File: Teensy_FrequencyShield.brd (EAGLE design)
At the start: 17 parts, among them IC9 78L05F

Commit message: Tweaked pin layout; added back in extra DDS & PLL channel names to Teensy pinout
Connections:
- net DDS3_CS: now also TEENSY.26; no longer TEENSY.15/A1
- net DDS3_IOUPDATE: now also TEENSY.28; no longer TEENSY.17/A3
- net DDS3_PS0: now also TEENSY.27; no longer TEENSY.16/A2
- net DDS3_RESET: now also TEENSY.25; no longer TEENSY.14/A0
- net PLL1_LE: now also TEENSY.15/A1; no longer TEENSY.30
- net PLL1_MUX: now also TEENSY.14/A0; no longer TEENSY.26
- net PLL2_LE: now also TEENSY.17/A3; no longer TEENSY.31
- net PLL2_MUX: now also TEENSY.16/A2; no longer TEENSY.27
- net PLL3_LE: now also TEENSY.30; no longer TEENSY.32
- net PLL3_MUX: now also TEENSY.29; no longer TEENSY.28
- net PLL4_LE: now also TEENSY.32; no longer TEENSY.33
- net PLL4_MUX: now also TEENSY.31; no longer TEENSY.29
- net SW1: now also TEENSY.33; no longer TEENSY.25
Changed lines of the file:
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@@
 <?xml version="1.0" encoding="utf-8"?>
 <!DOCTYPE eagle SYSTEM "eagle.dtd">
-<eagle version="6.2">
+<eagle version="6.5.0">
 <drawing>
 <settings>
@@
 </class>
 </classes>
-<designrules>
+<designrules name="default">
 <description language="de">&lt;b&gt;EAGLE Design Rules&lt;/b&gt;
 &lt;p&gt;
@@
 <signal name="PLL1_LE">
 <contactref element="PLL1" pad="3"/>
-<contactref element="TEENSY" pad="30"/>
-<wire x1="-20.32" y1="-5.08" x2="-19.05" y2="-26.67" width="0" layer="19" extent="1-1"/>
+<contactref element="TEENSY" pad="15/A1"/>
+<wire x1="-15.24" y1="-5.08" x2="-19.05" y2="-26.67" width="0" layer="19" extent="1-1"/>
 </signal>
 <signal name="PLL1_MUX">
 <contactref element="PLL1" pad="4"/>
-<contactref element="TEENSY" pad="26"/>
-<wire x1="-22.86" y1="-2.54" x2="-19.05" y2="-24.13" width="0" layer="19" extent="1-1"/>
+<contactref element="TEENSY" pad="14/A0"/>
+<wire x1="-15.24" y1="-7.62" x2="-19.05" y2="-24.13" width="0" layer="19" extent="1-1"/>
 </signal>
 <signal name="PLL2_LE">
 <contactref element="PLL2" pad="3"/>
-<contactref element="TEENSY" pad="31"/>
-<wire x1="6.35" y1="-26.67" x2="-20.32" y2="-2.54" width="0" layer="19" extent="1-1"/>
+<contactref element="TEENSY" pad="17/A3"/>
+<wire x1="-15.24" y1="0" x2="6.35" y2="-26.67" width="0" layer="19" extent="1-1"/>
 </signal>
 <signal name="PLL2_MUX">
 <contactref element="PLL2" pad="4"/>
-<contactref element="TEENSY" pad="27"/>
-<wire x1="6.35" y1="-24.13" x2="-22.86" y2="-5.08" width="0" layer="19" extent="1-1"/>
+<contactref element="TEENSY" pad="16/A2"/>
+<wire x1="-15.24" y1="-2.54" x2="6.35" y2="-24.13" width="0" layer="19" extent="1-1"/>
 </signal>
 <signal name="PLL3_LE">
 <contactref element="PLL3" pad="3"/>
-<contactref element="TEENSY" pad="32"/>
-<wire x1="31.75" y1="-26.67" x2="-20.32" y2="0" width="0" layer="19" extent="1-1"/>
+<contactref element="TEENSY" pad="30"/>
+<wire x1="31.75" y1="-26.67" x2="-20.32" y2="-5.08" width="0" layer="19" extent="1-1"/>
 </signal>
 <signal name="PLL3_MUX">
 <contactref element="PLL3" pad="4"/>
-<contactref element="TEENSY" pad="28"/>
-<wire x1="31.75" y1="-24.13" x2="-22.86" y2="-7.62" width="0" layer="19" extent="1-1"/>
+<contactref element="TEENSY" pad="29"/>
+<wire x1="31.75" y1="-24.13" x2="-20.32" y2="-7.62" width="0" layer="19" extent="1-1"/>
 </signal>
 <signal name="PLL4_LE">
 <contactref element="PLL4" pad="3"/>
-<contactref element="TEENSY" pad="33"/>
-<wire x1="-20.32" y1="2.54" x2="55.88" y2="-26.67" width="0" layer="19" extent="1-1"/>
+<contactref element="TEENSY" pad="32"/>
+<wire x1="-20.32" y1="0" x2="55.88" y2="-26.67" width="0" layer="19" extent="1-1"/>
 </signal>
 <signal name="PLL4_MUX">
 <contactref element="PLL4" pad="4"/>
-<contactref element="TEENSY" pad="29"/>
-<wire x1="-20.32" y1="-7.62" x2="55.88" y2="-24.13" width="0" layer="19" extent="1-1"/>
+<contactref element="TEENSY" pad="31"/>
+<wire x1="-20.32" y1="-2.54" x2="55.88" y2="-24.13" width="0" layer="19" extent="1-1"/>
 </signal>
 <signal name="DDS1_RESET">
@@
 <signal name="DDS3_RESET">
 <contactref element="DDS3" pad="15"/>
-<contactref element="TEENSY" pad="14/A0"/>
-<wire x1="-15.24" y1="-7.62" x2="74.93" y2="-25.4" width="0" layer="19" extent="1-1"/>
+<contactref element="TEENSY" pad="25"/>
+<wire x1="-22.86" y1="0" x2="74.93" y2="-25.4" width="0" layer="19" extent="1-1"/>
 </signal>
 <signal name="DDS3_CS">
 <contactref element="DDS3" pad="13"/>
-<contactref element="TEENSY" pad="15/A1"/>
-<wire x1="-15.24" y1="-5.08" x2="74.93" y2="-22.86" width="0" layer="19" extent="1-1"/>
+<contactref element="TEENSY" pad="26"/>
+<wire x1="-22.86" y1="-2.54" x2="74.93" y2="-22.86" width="0" layer="19" extent="1-1"/>
 </signal>
 <signal name="DDS4_RESET">
@@
 <signal name="DDS3_PS0">
 <contactref element="DDS3" pad="5"/>
-<contactref element="TEENSY" pad="16/A2"/>
-<wire x1="-15.24" y1="-2.54" x2="74.93" y2="-12.7" width="0" layer="19" extent="1-1"/>
+<contactref element="TEENSY" pad="27"/>
+<wire x1="-22.86" y1="-5.08" x2="74.93" y2="-12.7" width="0" layer="19" extent="1-1"/>
 </signal>
 <signal name="DDS3_IOUPDATE">
 <contactref element="DDS3" pad="1"/>
-<contactref element="TEENSY" pad="17/A3"/>
-<wire x1="-15.24" y1="0" x2="74.93" y2="-7.62" width="0" layer="19" extent="1-1"/>
+<contactref element="TEENSY" pad="28"/>
+<wire x1="-22.86" y1="-7.62" x2="74.93" y2="-7.62" width="0" layer="19" extent="1-1"/>
 </signal>
 <signal name="DDS4_IOUPDATE">
@@
 <signal name="SW1">
 <contactref element="ENC/SW" pad="3"/>
-<contactref element="TEENSY" pad="25"/>
-<wire x1="-22.86" y1="0" x2="-33.02" y2="29.21" width="0" layer="19" extent="1-1"/>
+<contactref element="TEENSY" pad="33"/>
+<wire x1="-33.02" y1="29.21" x2="-20.32" y2="2.54" width="0" layer="19" extent="1-1"/>
 </signal>
 <signal name="+5V">

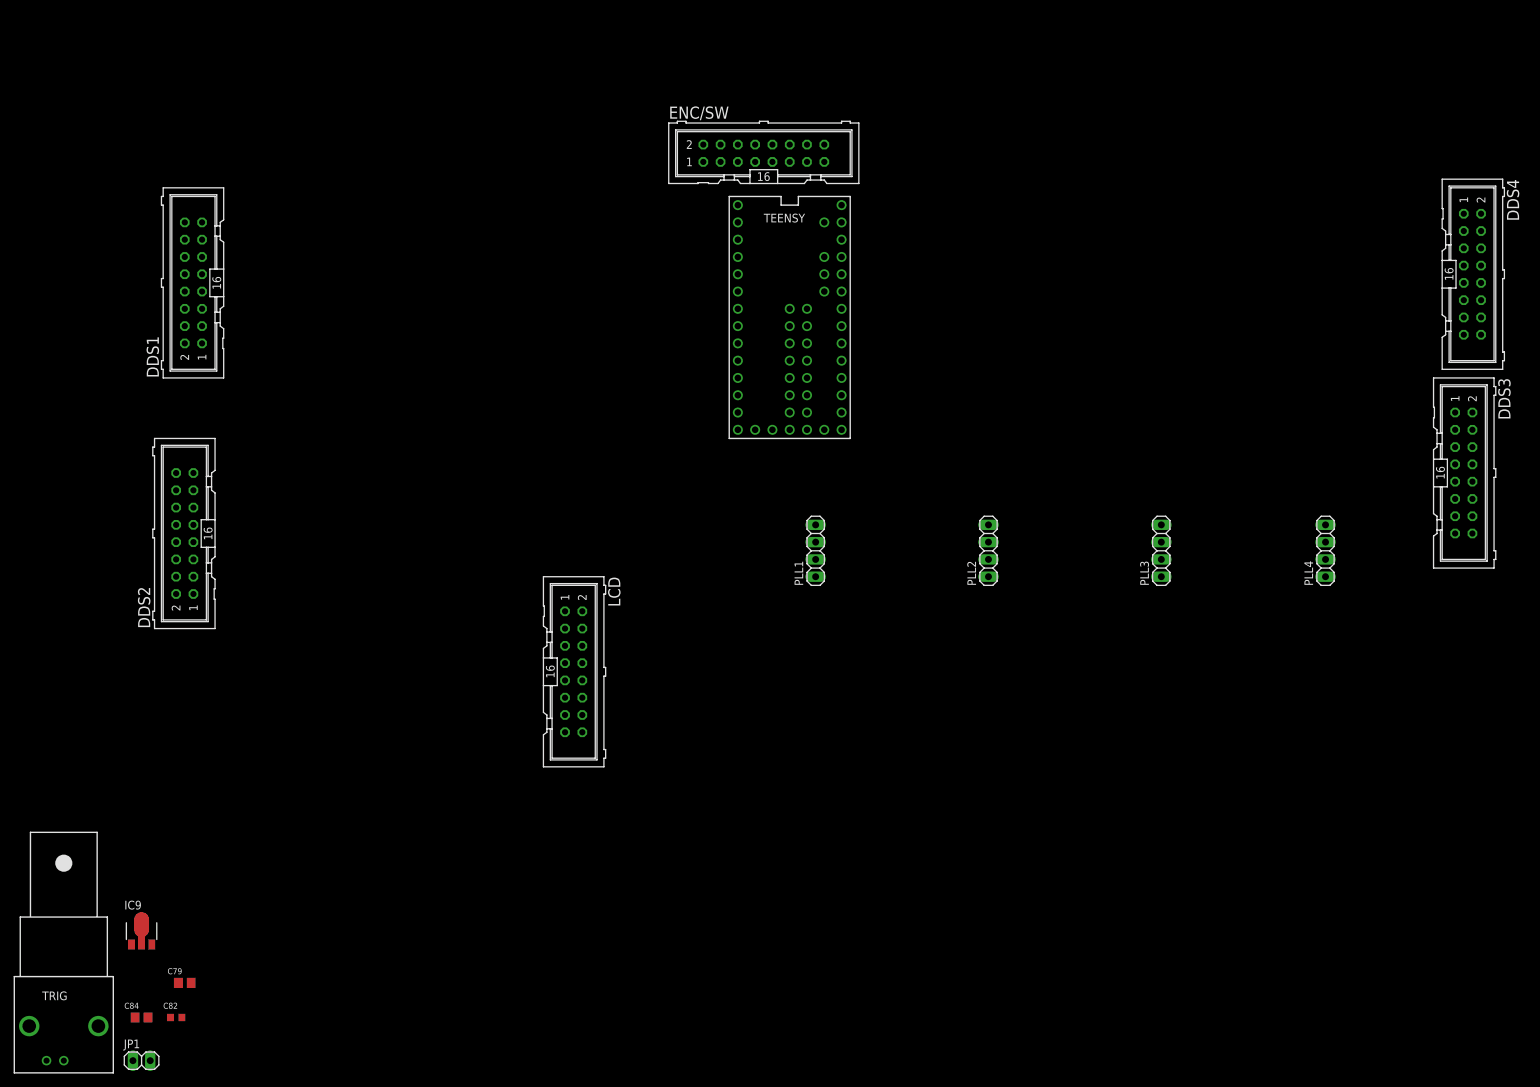
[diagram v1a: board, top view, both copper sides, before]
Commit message: Routed generic frequency breakout shield for teensy
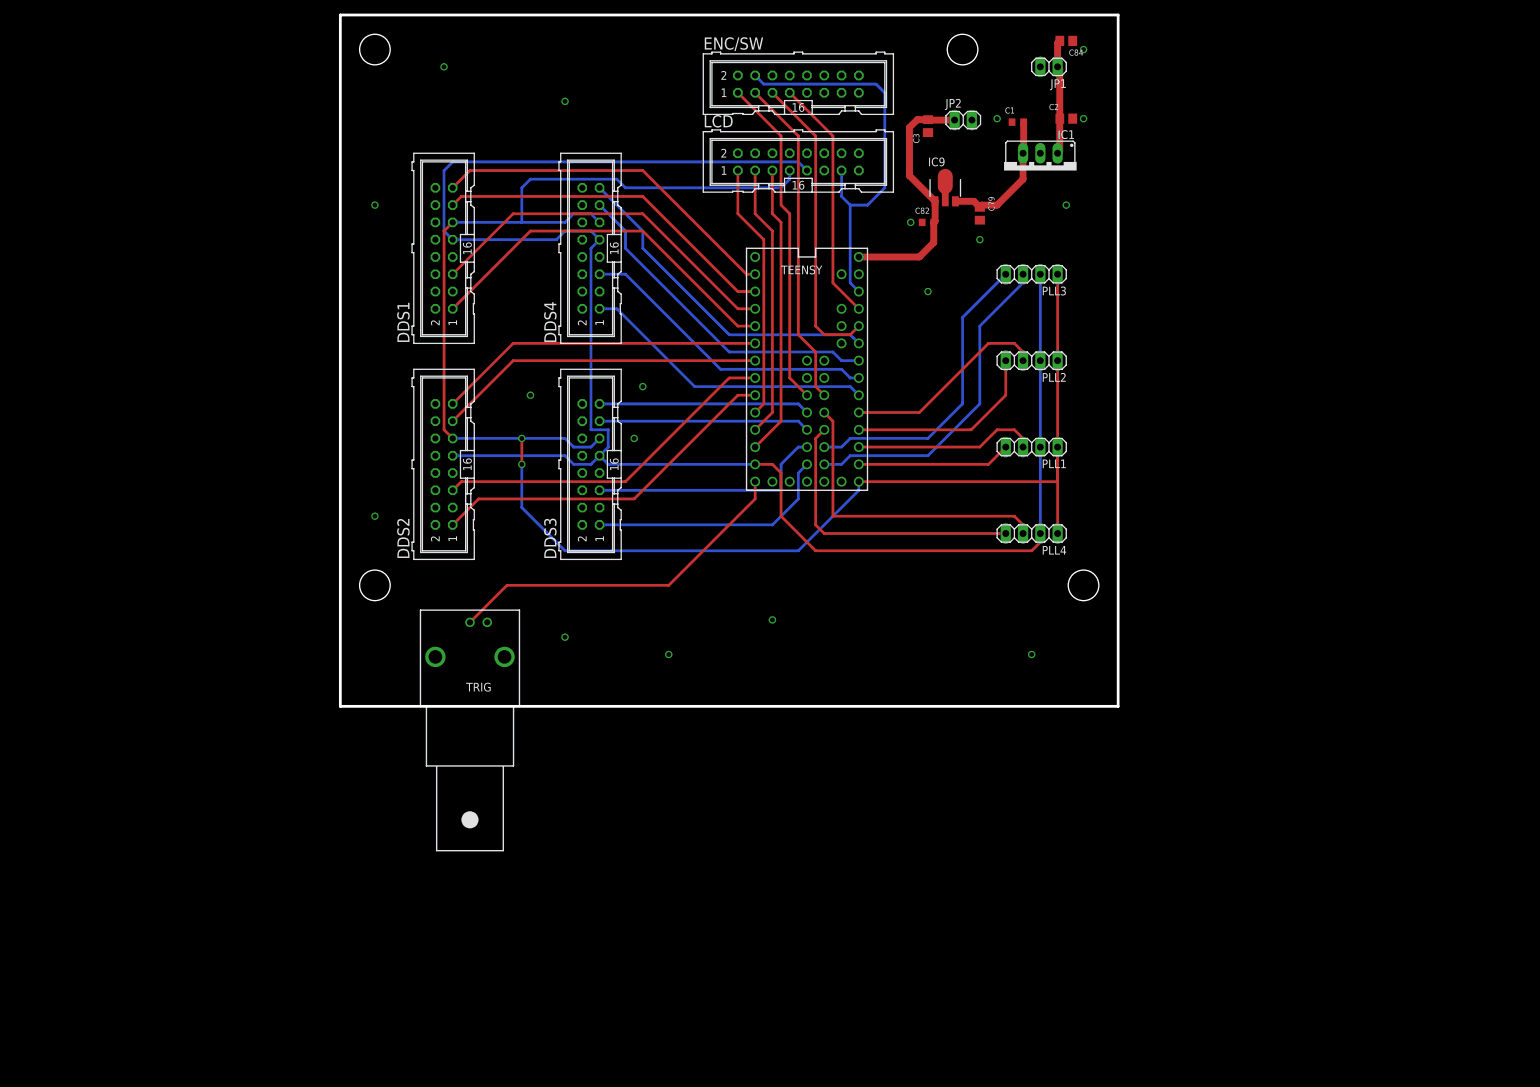
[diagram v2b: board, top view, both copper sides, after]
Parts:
- added C1: 100nF, rlc-jqi:0603
- added C2: 1uF, rlc-jqi:0805
- added C3: 10uF, rlc-jqi:0805
- added IC1: (no value), regulator-jqi:TO220
- added JP2: (no value), pinhead:1X02
- moved JP1 197.8 mm to (15.2, 43.2), turned to 180 degrees
- moved C84 197.6 mm to (17.8, 47.0), turned to 180 degrees
- moved C79 162.6 mm to (5.08, 21.6), turned to 270 degrees
- moved IC9 160.9 mm to (0.00, 25.4)
- moved C82 160.8 mm to (-2.54, 20.3)
- moved DDS4 129.6 mm to (-52.1, 16.5), turned to 90 degrees
- moved DDS3 128.3 mm to (-52.1, -15.2), turned to 90 degrees
- moved LCD 81.9 mm to (-21.6, 29.2), turned to 0 degrees
- moved TRIG 80.7 mm to (-69.8, -43.5), turned to 180 degrees
- moved PLL3 44.9 mm to (12.7, 12.7), turned to 180 degrees
- moved PLL4 43.3 mm to (12.7, -25.4), turned to 180 degrees
- moved DDS2 39.4 mm to (-73.7, -15.2)
- moved DDS1 37.2 mm to (-73.7, 16.5)
- moved PLL1 35.2 mm to (12.7, -12.7), turned to 180 degrees
- moved PLL2 28.7 mm to (12.7, 0.00), turned to 180 degrees
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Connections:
- removed net AGND: TEENSY.AGND
- new net N$2: C1.2, C79.1, IC1.3, IC9.3
- net +5V: now also C3.2, JP2.1
- net DDS4_CS: now also TEENSY.20/A6; no longer TEENSY.19/A5
- net DDS4_IOUPDATE: now also TEENSY.18/A4; no longer TEENSY.21/A7
- net DDS4_PS0: now also TEENSY.19/A5; no longer TEENSY.20/A6
- net DDS4_RESET: now also TEENSY.21/A7; no longer TEENSY.18/A4
- net ENC_A: now also TEENSY.23/A9; no longer TEENSY.22/A8
- net ENC_B: now also TEENSY.22/A8; no longer TEENSY.23/A9
- net GND: now also C1.1, C2.2, C3.1, IC1.2, JP2.2, TEENSY.AGND
- net PLL3_LE: now also TEENSY.29; no longer TEENSY.30
- net PLL3_MUX: now also TEENSY.30; no longer TEENSY.29
- net V+: now also C2.1, IC1.1; no longer C79.1, IC9.3
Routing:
- net CLK: track 0.00 -> 265.0 mm, vias 0 -> 2
- net MOSI: track 0.00 -> 261.1 mm
- net VDD: track 0.00 -> 59.0 mm
- net DDS1_IOUPDATE: track 0.00 -> 55.0 mm
- net DDS1_PS0: track 0.00 -> 53.9 mm
- net DDS2_IOUPDATE: track 0.00 -> 52.3 mm
- net SETLIST_TRIG: track 0.00 -> 52.0 mm
- net DDS1_RESET: track 0.00 -> 51.8 mm
- net DDS2_PS0: track 0.00 -> 51.3 mm
- net DDS1_CS: track 0.00 -> 50.8 mm
- net DDS4_RESET: track 0.00 -> 49.1 mm
- net DDS4_CS: track 0.00 -> 49.1 mm
- net SW1: track 0.00 -> 48.7 mm
- net ENC_SW: track 0.00 -> 48.7 mm
- net PLL3_LE: track 0.00 -> 48.2 mm
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- added copper zone on layer 1, net GND
- added copper zone on layer 16, net GND
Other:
- board outline added: 114.3 x 101.6 mm
